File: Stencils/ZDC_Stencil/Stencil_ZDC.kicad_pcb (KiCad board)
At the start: 2 copper layers, 134 x 89 mm, 46 parts

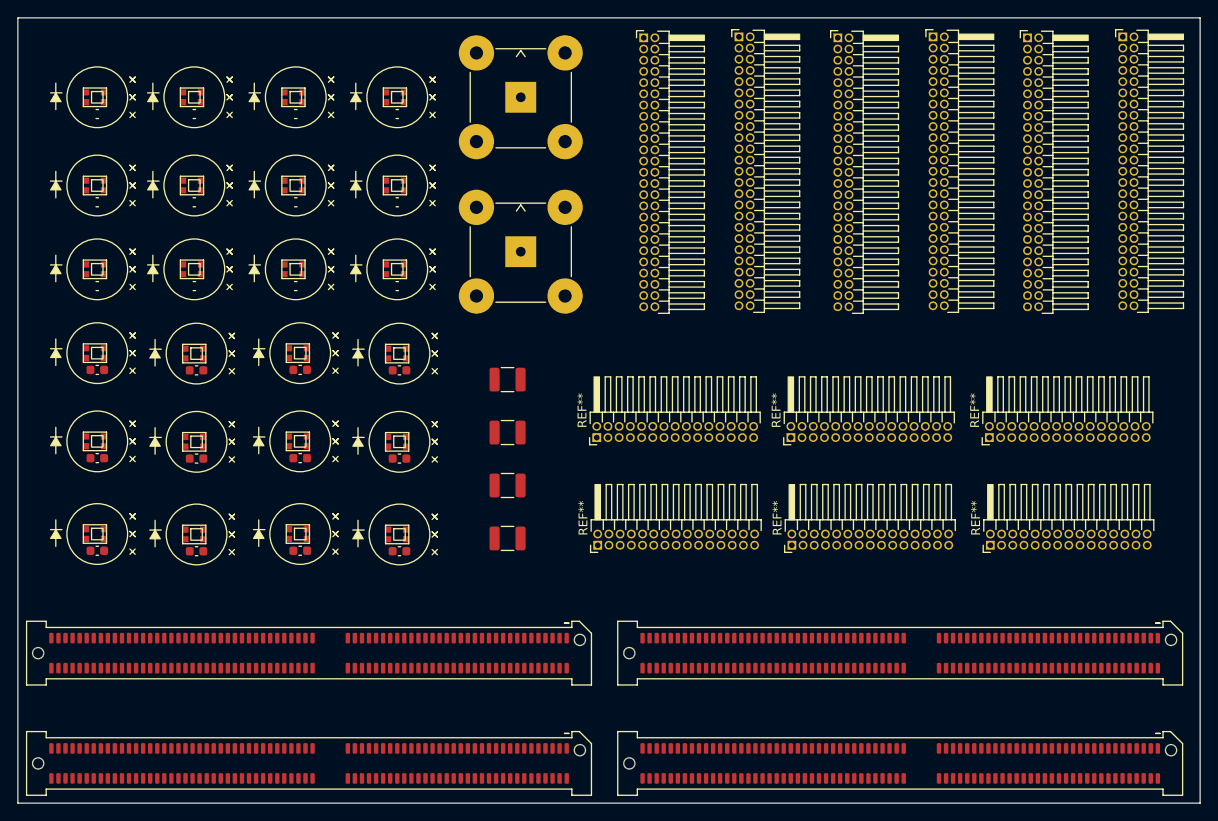
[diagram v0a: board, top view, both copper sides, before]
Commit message: Updated zdc stencil
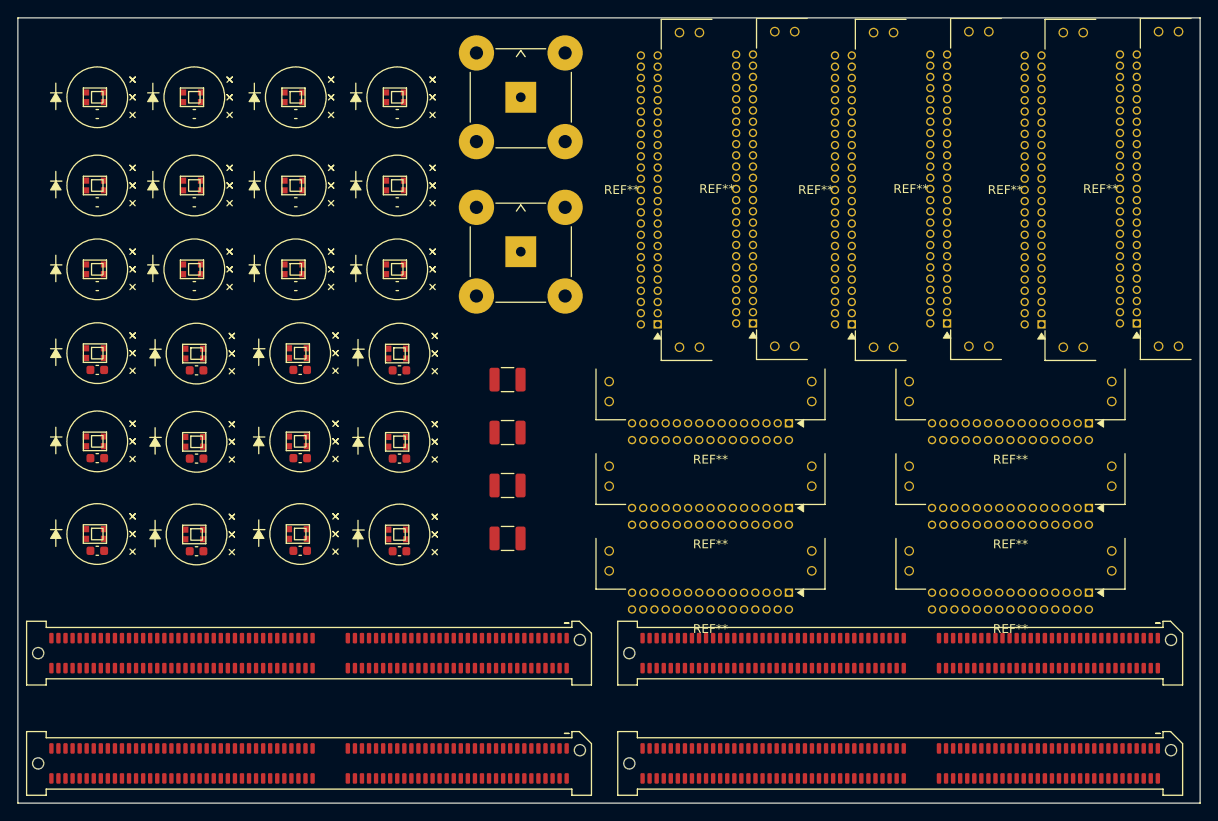
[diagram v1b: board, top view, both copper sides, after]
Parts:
- removed the REF** at (182.1, 89.1)
- removed the REF** at (204.7, 101.3)
- removed the REF** at (176.2, 43.6)
- removed the REF** at (208.9, 43.8)
- removed the REF** at (182.2, 101.3)
- removed the REF** at (160.2, 101.3)
- removed the REF** at (165.4, 43.8)
- removed the REF** at (219.7, 43.6)
- removed the REF** at (204.6, 89.1)
- removed the REF** at (160.1, 89.1)
- removed the REF** at (198.2, 43.6)
- removed the REF** at (187.4, 43.8)
- added REF**: Samtec_TFM-125-01-x-D-RE1-WT_2x25_P1.27mm_Horizontal, Samtec_TFM:Samtec_TFM-125-01-x-D-RE1-WT_2x25_P1.27mm_Horizontal, F.Cu at (188.1, 61.0)
- added REF**: Samtec_TFM-125-01-x-D-RE1-WT_2x25_P1.27mm_Horizontal, Samtec_TFM:Samtec_TFM-125-01-x-D-RE1-WT_2x25_P1.27mm_Horizontal, F.Cu at (166.1, 61.0)
- added REF**: Samtec_TFM-115-01-x-D-RE1-WT_2x15_P1.27mm_Horizontal, Samtec_TFM:Samtec_TFM-115-01-x-D-RE1-WT_2x15_P1.27mm_Horizontal, F.Cu at (173.0, 98.0)
- added REF**: Samtec_TFM-115-01-x-D-RE1-WT_2x15_P1.27mm_Horizontal, Samtec_TFM:Samtec_TFM-115-01-x-D-RE1-WT_2x15_P1.27mm_Horizontal, F.Cu at (173.0, 88.4)
- added REF**: Samtec_TFM-125-01-x-D-RE1-WT_2x25_P1.27mm_Horizontal, Samtec_TFM:Samtec_TFM-125-01-x-D-RE1-WT_2x25_P1.27mm_Horizontal, F.Cu at (209.6, 61.0)
- added REF**: Samtec_TFM-125-01-x-D-RE1-WT_2x25_P1.27mm_Horizontal, Samtec_TFM:Samtec_TFM-125-01-x-D-RE1-WT_2x25_P1.27mm_Horizontal, F.Cu at (220.4, 60.9)
- added REF**: Samtec_TFM-125-01-x-D-RE1-WT_2x25_P1.27mm_Horizontal, Samtec_TFM:Samtec_TFM-125-01-x-D-RE1-WT_2x25_P1.27mm_Horizontal, F.Cu at (198.9, 60.9)
- added REF**: Samtec_TFM-115-01-x-D-RE1-WT_2x15_P1.27mm_Horizontal, Samtec_TFM:Samtec_TFM-115-01-x-D-RE1-WT_2x15_P1.27mm_Horizontal, F.Cu at (173.0, 107.6)
- added REF**: Samtec_TFM-125-01-x-D-RE1-WT_2x25_P1.27mm_Horizontal, Samtec_TFM:Samtec_TFM-125-01-x-D-RE1-WT_2x25_P1.27mm_Horizontal, F.Cu at (176.9, 60.9)
- added REF**: Samtec_TFM-115-01-x-D-RE1-WT_2x15_P1.27mm_Horizontal, Samtec_TFM:Samtec_TFM-115-01-x-D-RE1-WT_2x15_P1.27mm_Horizontal, F.Cu at (207.0, 107.6)
- added REF**: Samtec_TFM-115-01-x-D-RE1-WT_2x15_P1.27mm_Horizontal, Samtec_TFM:Samtec_TFM-115-01-x-D-RE1-WT_2x15_P1.27mm_Horizontal, F.Cu at (207.0, 88.4)
- added REF**: Samtec_TFM-115-01-x-D-RE1-WT_2x15_P1.27mm_Horizontal, Samtec_TFM:Samtec_TFM-115-01-x-D-RE1-WT_2x15_P1.27mm_Horizontal, F.Cu at (207.0, 98.0)
